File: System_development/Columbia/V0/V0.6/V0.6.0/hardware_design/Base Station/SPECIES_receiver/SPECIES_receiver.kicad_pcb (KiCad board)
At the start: 2 copper layers, 146.4 x 73.5 mm, 8 parts, among them J1 nRF 1, J2 nRF 2, J3 Raspb Pi

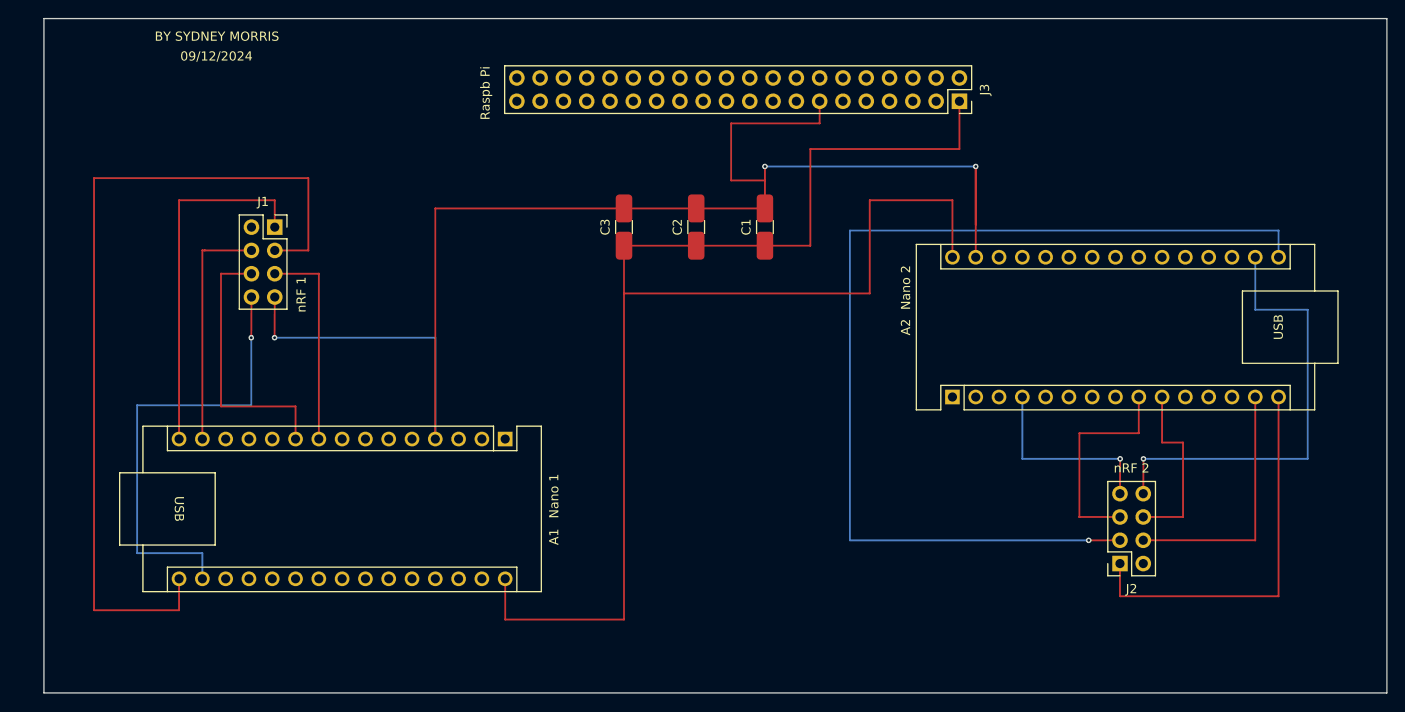
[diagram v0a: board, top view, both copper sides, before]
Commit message: updated base station receiver pcb
decreased board size, flipped nRF pinout, and added clearer silkscreen labels
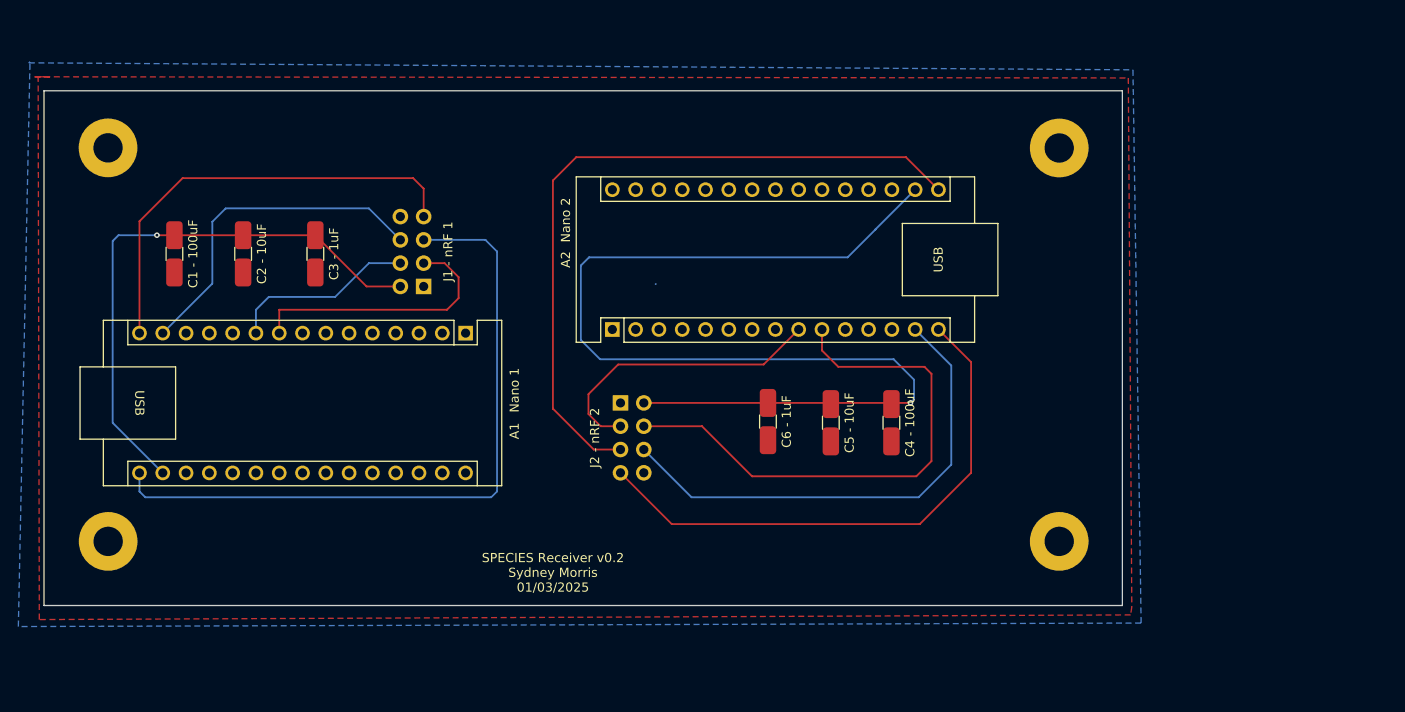
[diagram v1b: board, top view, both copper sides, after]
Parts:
- removed J3: Raspb Pi, Connector_PinSocket_2.54mm:PinSocket_2x20_P2.54mm_Vertical
- added C4 - 100uF: C_Small, SPECIES_Elongated:C_1206_3216Metric, F.Cu at (156.2, 82.0)
- added C5 - 10uF: C_Small, SPECIES_Elongated:C_1206_3216Metric, F.Cu at (149.6, 82.0)
- added C6 - 1uF: C_Small, SPECIES_Elongated:C_1206_3216Metric, F.Cu at (142.7, 81.9)
- added G***: LOGO, digikey-footprints:artslogo, B.Cu at (123.3, 72.3)
- added REF**: MountingHole_3.2mm_M3_Pad, MountingHole:MountingHole_3.2mm_M3_Pad, F.Cu at (70.8, 95.0)
- added REF**: MountingHole_3.2mm_M3_Pad, MountingHole:MountingHole_3.2mm_M3_Pad, F.Cu at (70.7, 52.1)
- added REF**: MountingHole_3.2mm_M3_Pad, MountingHole:MountingHole_3.2mm_M3_Pad, F.Cu at (174.5, 52.1)
- added REF**: MountingHole_3.2mm_M3_Pad, MountingHole:MountingHole_3.2mm_M3_Pad, F.Cu at (174.5, 95.0)
- C1 - 100uF: renamed from C1
- C2 - 10uF: renamed from C2
- C3 - 1uF: renamed from C3
- J1: value nRF 1 -> Conn_02x04_Odd_Even_MountingPin; moved to B.Cu
- J2: value nRF 2 -> Conn_02x04_Odd_Even_MountingPin; moved to B.Cu
- moved C1 - 100uF 64.5 mm to (78.0, 63.6), turned to -90 degrees
- moved J2 57.2 mm to (126.6, 79.9)
- moved C2 - 10uF 49.5 mm to (85.5, 63.6), turned to -90 degrees
- moved A2 37.8 mm to (125.7, 71.9)
- moved C3 - 1uF 33.8 mm to (93.3, 63.6), turned to -90 degrees
- moved J1 17.5 mm to (105.2, 67.2)
- moved A1 12.3 mm to (109.7, 72.3)
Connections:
- A1 pad 30: Net-(A1-VIN) -> unconnected-(A1-VIN-Pad30)
- A2 pad 27: Net-(A1-VIN) -> Net-(A2-+5V)
- A2 pad 29: GND -> unconnected-(A2-GND-Pad29)
- A2 pad 30: Net-(A1-VIN) -> Net-(A2-+5V)
- C1 - 100uF pad 1: Net-(A1-VIN) -> 3V3
- C2 - 10uF pad 1: Net-(A1-VIN) -> 3V3
- C3 - 1uF pad 1: Net-(A1-VIN) -> 3V3
- J1 pad 1: unconnected-(J1-Pin_1-Pad1) -> GND
- J1 pad 2: unconnected-(J1-Pin_2-Pad2) -> 3V3
- J1 pad 3: unconnected-(J1-Pin_3-Pad3) -> CE
- J1 pad 4: unconnected-(J1-Pin_4-Pad4) -> CSN
- J1 pad 5: unconnected-(J1-Pin_5-Pad5) -> CLK
- J1 pad 6: unconnected-(J1-Pin_6-Pad6) -> MOSI
- J1 pad 7: unconnected-(J1-Pin_7-Pad7) -> MISO
- J2 pad 1: MISO -> GND
- J2 pad 2: unconnected-(J2-Pin_2-Pad2) -> 3V3
- J2 pad 3: CLK -> CE
- J2 pad 4: MOSI -> CSN
- J2 pad 5: CE -> CLK
- J2 pad 6: CSN -> MOSI
- J2 pad 7: GND -> MISO
- J2 pad 8: 3V3 -> unconnected-(J2-Pin_8-Pad8)
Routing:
- net GND: track 181.3 -> 0.00 mm, vias 4 -> 0
- net Net-(A1-VIN): track 162.7 -> 0.00 mm
- net 3V3: track 99.9 -> 179.4 mm
- net CLK: track 207.6 -> 154.9 mm, vias 1 -> 0
- net MOSI: track 53.8 -> 90.4 mm
- net CSN: track 49.2 -> 79.5 mm
- net MISO: track 82.0 -> 108.6 mm
- net CE: track 46.8 -> 61.4 mm
- added copper zone on B.Cu, net GND
- added copper zone on F.Cu, net GND
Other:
- board size 146.4 x 73.5 mm -> 117.6 x 56.1 mm
- board text added: "ARTS Lab University of South Carolina"
- board text added: "J1 - nRF 1"
- board text added: "J2 - nRF 2"
- board text added: "SPECIES Receiver v0.2 Sydney Morris 01/03/2025"
- board text removed: "09/12/2024"
- board text removed: "BY SYDNEY MORRIS"
